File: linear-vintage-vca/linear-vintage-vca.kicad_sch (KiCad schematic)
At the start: 57 parts, among them J1 Conn_02x08_Odd_Even, J10 Conn_01x02_Pin, J11 Conn_01x02_Pin, J2 AudioJack2, J3 AudioJack2, J4 AudioJack2, J5 AudioJack2, J6 AudioJack2, J7 AudioJack2, J8 AudioJack2, J9 AudioJack2, Q1 BC556, Q2 BC556, SW1 SW_SPDT_321, SW2 SW_SPDT_321, U1 LM13700, U2 TL072, U3 TL072

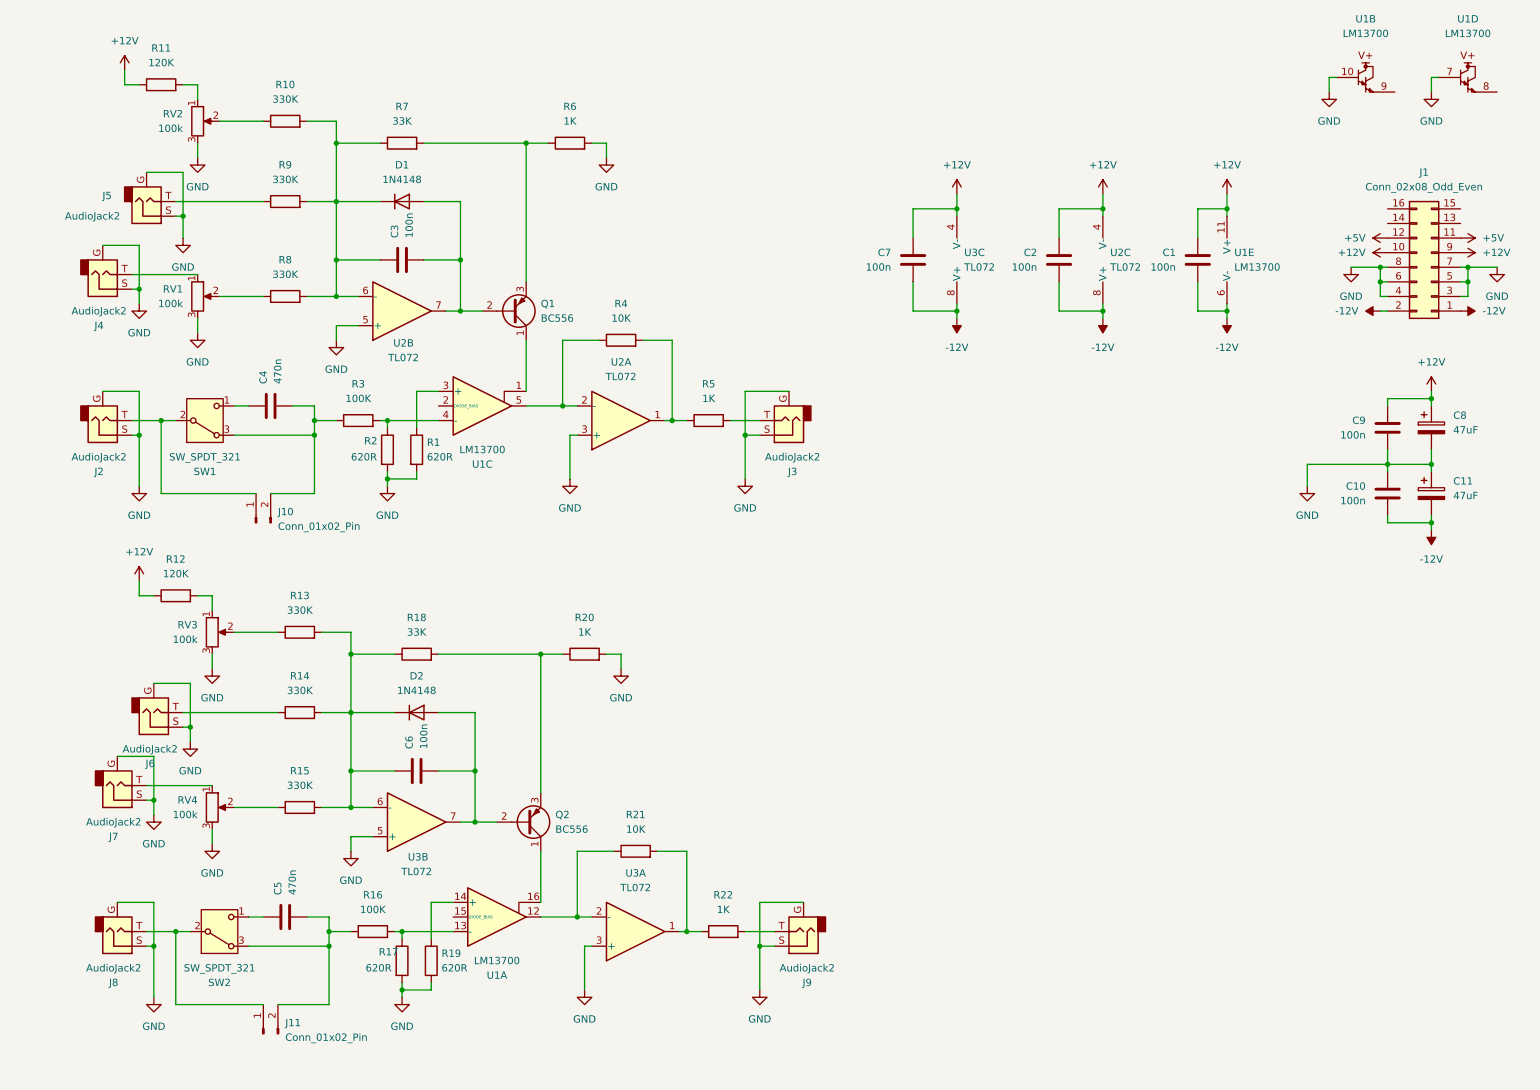
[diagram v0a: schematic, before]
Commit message: Linear VCA mismatched TL072 power supply fixed.
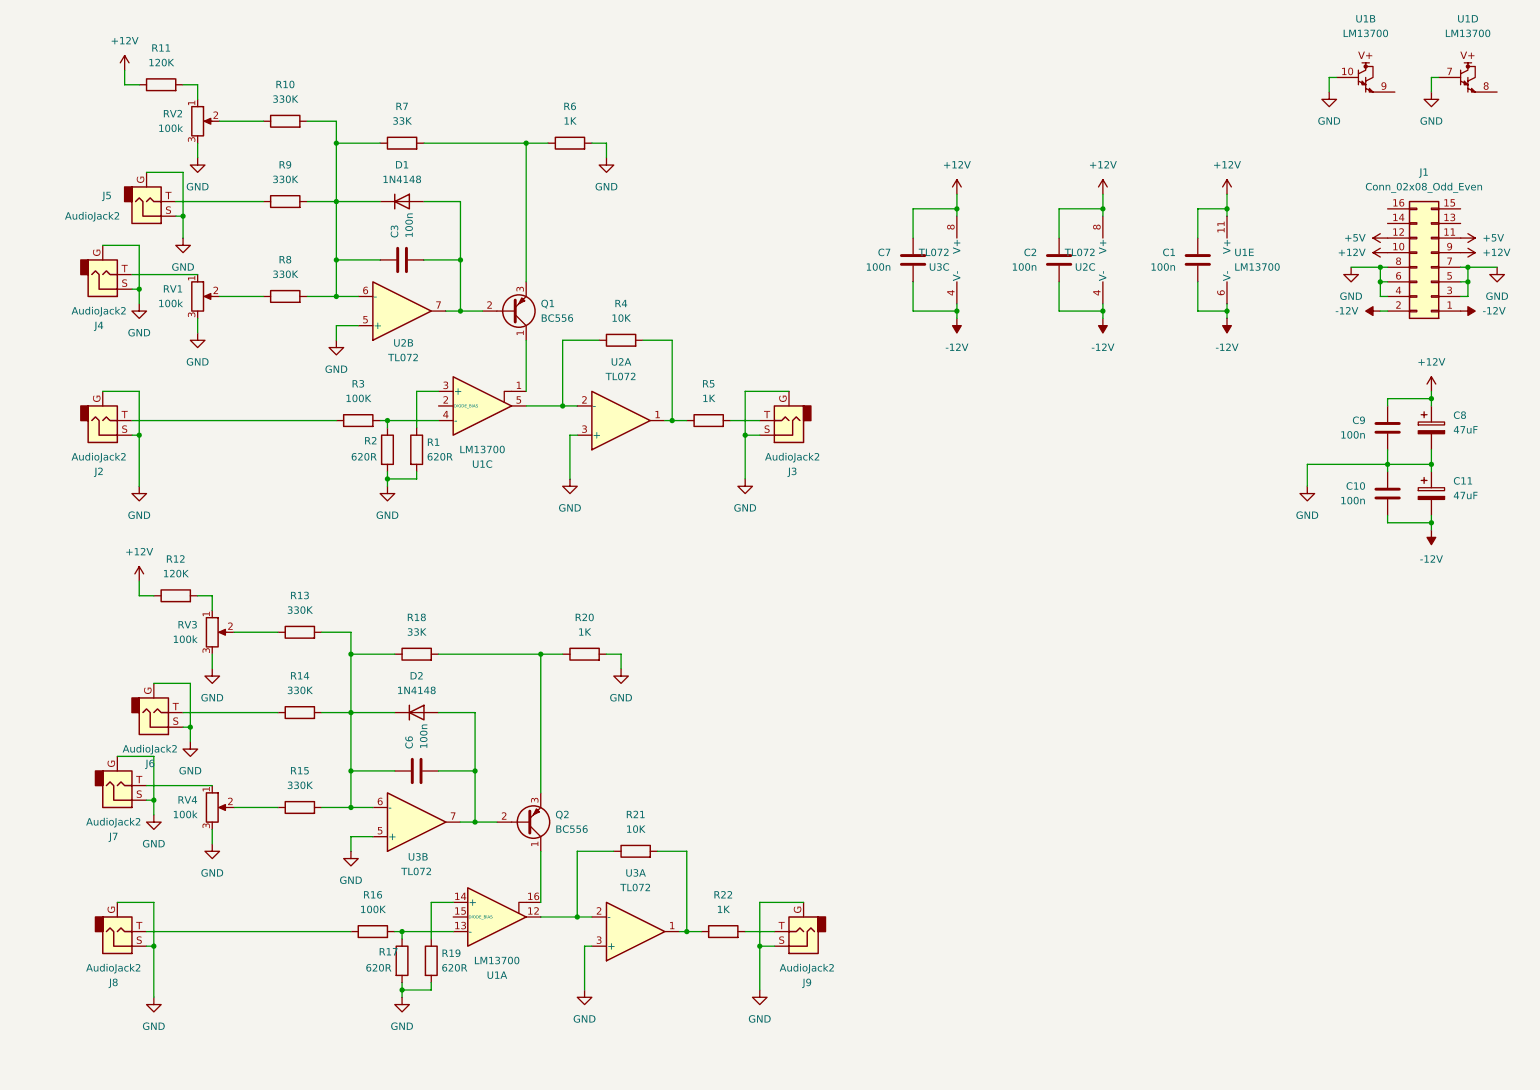
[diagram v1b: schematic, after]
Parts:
- removed C4, C5: 470n, Capacitor_THT:C_Rect_L7.0mm_W2.0mm_P5.00mm, symbol Device:C
- removed J10, J11: Conn_01x02_Pin, Connector_PinHeader_2.54mm:PinHeader_2x01_P2.54mm_Vertical, symbol Connector:Conn_01x02_Pin
- removed SW1, SW2: SW_SPDT_321, linear_vintage_vca:SPDT_MS-500, symbol Switch:SW_SPDT_321
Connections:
- net +12V: now also U2.8 (V+), U3.8 (V+); no longer U2.4 (V-), U3.4 (V-)
- net -12V: now also U2.4 (V-), U3.4 (V-); no longer U2.8 (V+), U3.8 (V+)
- net at R16.1: now also J8.T
- net at J2.T: now also R3.1
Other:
- moved on the sheet: U2C, U3C

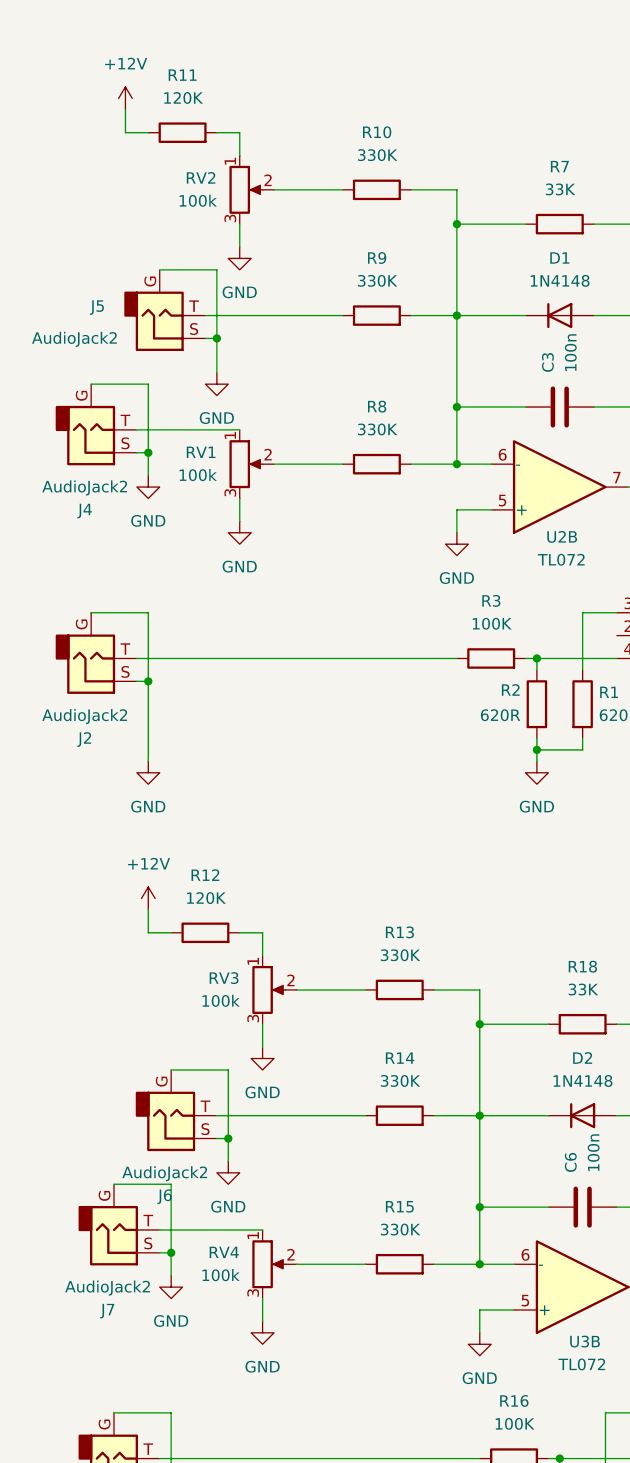
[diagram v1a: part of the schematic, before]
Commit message: Fixed OpAmp power rails.
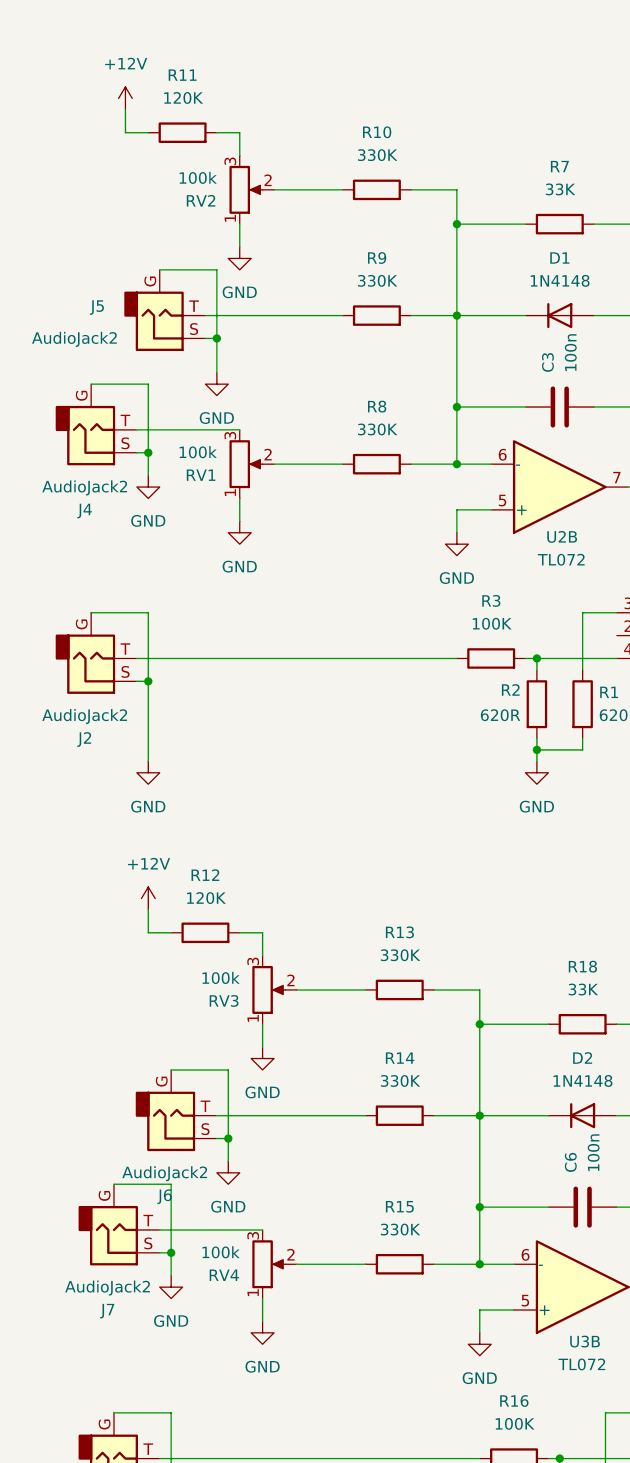
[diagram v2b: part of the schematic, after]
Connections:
- net GND: now also RV1.1, RV2.1, RV3.1, RV4.1; no longer RV1.3, RV2.3, RV3.3, RV4.3
- net at R11.2: now also RV2.3; no longer RV2.1
- net at J7.T: now also RV4.3; no longer RV4.1
- net at R12.2: now also RV3.3; no longer RV3.1
- net at J4.T: now also RV1.3; no longer RV1.1
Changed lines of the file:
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@@
 		(lib_id "Device:R_Potentiometer")
 		(at 46.99 33.02 0)
+		(mirror x)
 		(unit 1)
 		(exclude_from_sim no)
@@
 		(on_board yes)
 		(dnp no)
-		(fields_autoplaced yes)
 		(property "Reference" "RV2"
-			(at 44.45 31.7499 0)
+			(at 44.45 34.2901 0)
 			(effects
 				(font
@@
 		)
 		(property "Value" "100k"
-			(at 44.45 34.2899 0)
+			(at 44.45 31.7501 0)
 			(effects
 				(font
@@
 		(lib_id "Device:R_Potentiometer")
 		(at 49.53 121.92 0)
+		(mirror x)
 		(unit 1)
 		(exclude_from_sim no)
@@
 		(on_board yes)
 		(dnp no)
-		(fields_autoplaced yes)
 		(property "Reference" "RV3"
-			(at 46.99 120.6499 0)
+			(at 46.99 123.1901 0)
 			(effects
 				(font
@@
 		)
 		(property "Value" "100k"
-			(at 46.99 123.1899 0)
+			(at 46.99 120.6501 0)
 			(effects
 				(font
@@
 		(lib_id "Device:R_Potentiometer")
 		(at 49.53 152.4 0)
+		(mirror x)
 		(unit 1)
 		(exclude_from_sim no)
@@
 		(on_board yes)
 		(dnp no)
-		(fields_autoplaced yes)
 		(property "Reference" "RV4"
-			(at 46.99 151.1299 0)
+			(at 46.99 153.6701 0)
 			(effects
 				(font
@@
 		)
 		(property "Value" "100k"
-			(at 46.99 153.6699 0)
+			(at 46.99 151.1301 0)
 			(effects
 				(font
@@
 		(lib_id "Device:R_Potentiometer")
 		(at 46.99 63.5 0)
+		(mirror x)
 		(unit 1)
 		(exclude_from_sim no)
@@
 		(on_board yes)
 		(dnp no)
-		(fields_autoplaced yes)
 		(property "Reference" "RV1"
-			(at 44.45 62.2299 0)
+			(at 44.45 64.7701 0)
 			(effects
 				(font
@@
 		)
 		(property "Value" "100k"
-			(at 44.45 64.7699 0)
+			(at 44.45 62.2301 0)
 			(effects
 				(font

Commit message: VCA v. 2.0
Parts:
- removed C2: 100n, Capacitor_THT:C_Rect_L7.0mm_W2.0mm_P5.00mm, symbol Device:C
- removed U2, U3: TL072, Package_DIP:DIP-8_W7.62mm_Socket, symbol Amplifier_Operational:TL072
- added C6, C8: 100n, Capacitor_THT:C_Rect_L7.0mm_W2.0mm_P5.00mm, symbol Device:C
- added J10, J9: Conn_01x10_Socket, Connector_PinSocket_2.54mm:PinSocket_1x06_P2.54mm_Vertical, symbol Connector:Conn_01x06_Socket
- added J11: Conn_01x04_Pin, Connector_PinHeader_2.54mm:PinHeader_1x04_P2.54mm_Vertical, symbol Connector:Conn_01x04_Pin
- added J12: Conn_01x04_Socket, Connector_PinSocket_2.54mm:PinSocket_1x04_P2.54mm_Vertical, symbol Connector:Conn_01x04_Socket
- added J7, J8: Conn_01x06_Pin, Connector_PinHeader_2.54mm:PinHeader_1x06_P2.54mm_Vertical, symbol Connector:Conn_01x06_Pin
- added JP1: SolderJumper_2_Open, Jumper:SolderJumper-2_P1.3mm_Open_RoundedPad1.0x1.5mm, symbol Jumper:SolderJumper_2_Open
- added TP1, TP2, TP3, TP4: TestPoint, TestPoint:TestPoint_Loop_D2.54mm_Drill1.5mm_Beaded, symbol Connector:TestPoint
- added U1: TL074, Package_DIP:DIP-14_W7.62mm_Socket_LongPads, symbol Amplifier_Operational:TL074
- J1: renamed from J4; footprint linear_vintage_vca:Jack_3.5mm_PJ-341-2_Vertical -> linear_vintage_vca:Jack_3.5mm_Switch; symbol Connector_Audio:AudioJack2_Ground -> linear_vintage_vca:AudioJack_Switch
- J13: renamed from J3; footprint linear_vintage_vca:Jack_3.5mm_PJ-341-2_Vertical -> linear_vintage_vca:Jack_3.5mm_Switch; symbol Connector_Audio:AudioJack2_Ground -> linear_vintage_vca:AudioJack_Switch
- J14: renamed from J9; footprint linear_vintage_vca:Jack_3.5mm_PJ-341-2_Vertical -> linear_vintage_vca:Jack_3.5mm_Switch; symbol Connector_Audio:AudioJack2_Ground -> linear_vintage_vca:AudioJack_Switch
- J2, J5, J6: footprint linear_vintage_vca:Jack_3.5mm_PJ-341-2_Vertical -> linear_vintage_vca:Jack_3.5mm_Switch; symbol Connector_Audio:AudioJack2_Ground -> linear_vintage_vca:AudioJack_Switch
- J3: renamed from J7; footprint linear_vintage_vca:Jack_3.5mm_PJ-341-2_Vertical -> linear_vintage_vca:Jack_3.5mm_Switch; symbol Connector_Audio:AudioJack2_Ground -> linear_vintage_vca:AudioJack_Switch
- J4: renamed from J8; footprint linear_vintage_vca:Jack_3.5mm_PJ-341-2_Vertical -> linear_vintage_vca:Jack_3.5mm_Switch; symbol Connector_Audio:AudioJack2_Ground -> linear_vintage_vca:AudioJack_Switch
- Q1, Q2: footprint Package_TO_SOT_THT:TO-92_Inline -> Package_TO_SOT_THT:TO-92_Inline_Wide
- U3: renamed from U1; footprint Package_DIP:DIP-16_W7.62mm_Socket -> Package_DIP:DIP-16_W7.62mm_Socket_LongPads
- renumbered C3 to C1, C8 to C11, C11 to C12, C6 to C2, C7 to C5, C1 to C7, J1 to J15, R11 to R1, R16 to R10, R2 to R11, R17 to R12, R7 to R13, R18 to R14, R1 to R15, R19 to R16, R6 to R17, R20 to R18, R4 to R19, R12 to R2, R21 to R20, R5 to R21, R10 to R3, R9 to R4, R8 to R5, R13 to R6, R14 to R7, R15 to R8, R3 to R9, RV2 to RV1, RV1 to RV2
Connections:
- net +12V: now also J12.4 (Pin_4), U1.4 (V+); no longer R1.1, R2.1
- net -12V: now also C6.2, C8.2, U1.11 (V-); no longer C5.2, C7.2
- net GND: now also C5.2, C7.2, C6.1, C8.1, J10.6 (Pin_6), J12.2 (Pin_2), J12.3 (Pin_3), J9.6 (Pin_6), U1.10 (+), U1.12 (+), U1.3 (+), U1.5 (+); no longer J1.G, J1.S, J13.G, J13.S, J14.G, J14.S, J2.G, J2.S, J3.G, J3.S, J4.G, J4.S, J5.G, J5.S, J6.G, J6.S, RV1.1, RV2.1, RV3.1, RV4.1, U3.10, U3.7
- net at R10.1: now also J10.5 (Pin_5); no longer J4.T
- net at RV1.2: now also J7.1 (Pin_1); no longer R3.1
- net at J6.T: now also J8.2 (Pin_2); no longer R7.1
- net at J2.T: now also J7.5 (Pin_5); no longer R9.1
- net at C2.1, D2.1 (K), R14.1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: now also U1.13 (-)
- net at Q2.3 (E), R14.2, R18.1: now also TP4.1
- net at R4.1: now also J9.2 (Pin_2); no longer J5.T
- net at C1.1, D1.1 (K), R13.1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: now also U1.2 (-)
- net at R19.1, U3.5: now also U1.6 (-)
- net at R19.2, R21.1: now also U1.7
- net at R20.2, R22.1: now also U1.8
- net OUT_2A: now reaches J14.T
- net OUT_2A: now also J8.4 (Pin_4); no longer R22.2
- net at R5.1: now also J9.3 (Pin_3); no longer RV2.2
- net at C1.2, D1.2 (A), Q1.2 (B): now also TP1.1, U1.1
- net at RV3.2: now also J8.1 (Pin_1); no longer R6.1
- net at RV4.2: now also J8.3 (Pin_3); no longer R8.1
- net at Q1.3 (E), R13.2, R17.1: now also TP3.1
- net at C2.2, D2.2 (A), Q2.2 (B): now also TP2.1, U1.14
- net CV_B: now reaches J15.13 (Pin_13)
- net CV_B: now also J15.14 (Pin_14), JP1.2 (B)
- net at R20.1, U3.12: now also U1.9 (-)
- net OUT_1A: now reaches J13.T
- net OUT_1A: now also J7.4 (Pin_4); no longer R21.2
- new net: J9.1 (Pin_1), R3.1
- new net: J9.5 (Pin_5), R9.1
- new net: J10.2 (Pin_2), R7.1
- new net: J10.1 (Pin_1), R6.1
- new net: J10.3 (Pin_3), R8.1
- new net: J4.T, J8.5 (Pin_5)
- new net: J12.1 (Pin_1), JP1.1 (A)
- new net: J7.3 (Pin_3), RV2.2
- new net: J5.T, J7.2 (Pin_2)
- new net +12V_A: J11.4 (Pin_4), R1.1, R2.1
- new net CV_A: J1.TN, J11.1 (Pin_1), J3.TN
- new net GND_A: J1.S, J11.2 (Pin_2), J11.3 (Pin_3), J13.S, J14.S, J2.S, J2.TN, J3.S, J4.S, J4.TN, J5.S, J5.TN, J6.S, J6.TN, J7.6 (Pin_6), J8.6 (Pin_6), RV1.1, RV2.1, RV3.1, RV4.1
- new net OUT_1B: J9.4 (Pin_4), R21.2
- new net OUT_2B: J10.4 (Pin_4), R22.2
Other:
- moved on the sheet: C1, C10, C11, C12, C2, C5, C7, C9, D1, D2, Q1, Q2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

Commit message: Updated VCA-1 panel
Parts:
- C1, C2: value 100n -> 1n
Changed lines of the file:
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@@
 			)
 		)
-		(property "Value" "100n"
+		(property "Value" "1n"
 			(at 116.8399 53.34 0)
 			(effects
@@
 			)
 		)
-		(property "Value" "100n"
+		(property "Value" "1n"
 			(at 116.8399 142.24 0)
 			(effects

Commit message: Front panel and output gain fix.
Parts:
- R19, R20: value 10K -> 20k
- TP4: footprint TestPoint:TestPoint_Loop_D2.54mm_Drill1.5mm_Beaded -> TestPoint:TestPoint_Loop_D1.80mm_Drill1.0mm_Beaded
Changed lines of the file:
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@@
 			)
 		)
-		(property "Value" "10K"
+		(property "Value" "20k"
 			(at 153.67 67.31 90)
 			(effects
@@
 			)
 		)
-		(property "Footprint" "TestPoint:TestPoint_Loop_D2.54mm_Drill1.5mm_Beaded"
+		(property "Footprint" "TestPoint:TestPoint_Loop_D1.80mm_Drill1.0mm_Beaded"
 			(at 142.24 125.73 0)
 			(effects
@@
 			)
 		)
-		(property "Value" "10K"
+		(property "Value" "20k"
 			(at 153.67 156.21 90)
 			(effects

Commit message: Simulated exponential VCA control stage
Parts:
- TP1, TP2: footprint TestPoint:TestPoint_Loop_D2.54mm_Drill1.5mm_Beaded -> TestPoint:TestPoint_Loop_D1.80mm_Drill1.0mm_Beaded
- TP3: footprint TestPoint:TestPoint_Loop_D2.54mm_Drill1.5mm_Beaded -> TestPoint:TestPoint_Loop_D2.50mm_Drill1.0mm
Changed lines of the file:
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@@
 			)
 		)
-		(property "Footprint" "TestPoint:TestPoint_Loop_D2.54mm_Drill1.5mm_Beaded"
+		(property "Footprint" "TestPoint:TestPoint_Loop_D1.80mm_Drill1.0mm_Beaded"
 			(at 120.65 154.94 0)
 			(effects
@@
 			)
 		)
-		(property "Footprint" "TestPoint:TestPoint_Loop_D2.54mm_Drill1.5mm_Beaded"
+		(property "Footprint" "TestPoint:TestPoint_Loop_D2.50mm_Drill1.0mm"
 			(at 142.24 36.83 0)
 			(effects
@@
 			)
 		)
-		(property "Footprint" "TestPoint:TestPoint_Loop_D2.54mm_Drill1.5mm_Beaded"
+		(property "Footprint" "TestPoint:TestPoint_Loop_D1.80mm_Drill1.0mm_Beaded"
 			(at 120.65 66.04 0)
 			(effects
